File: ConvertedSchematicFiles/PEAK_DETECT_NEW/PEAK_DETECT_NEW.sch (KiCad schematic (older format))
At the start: 17 parts, among them U1 uA741

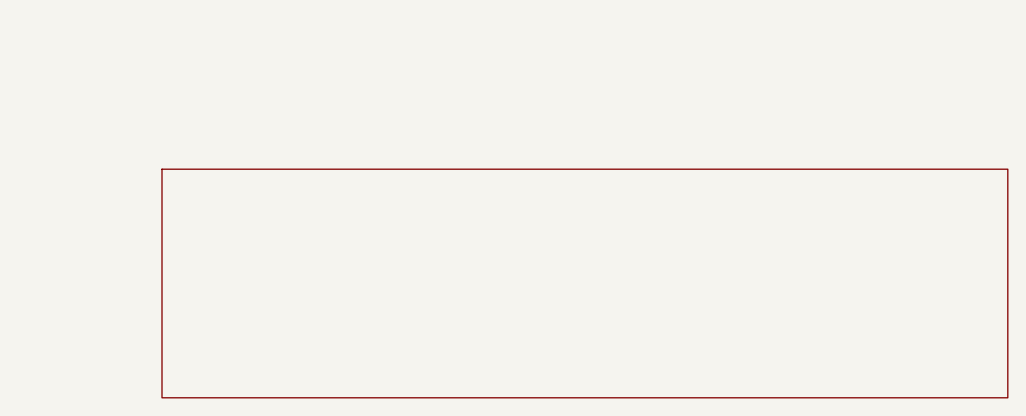
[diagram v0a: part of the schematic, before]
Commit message: Excluded some components. These no longer appear after conversion. When calling shell commands, filenames are in "quotes"
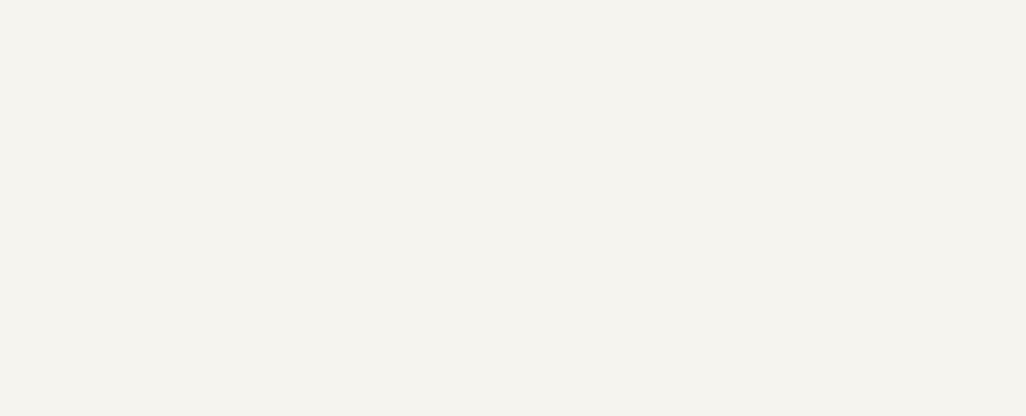
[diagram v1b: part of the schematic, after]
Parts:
- removed titleblk: titleblk, symbol TITLEBLK_PSPICE
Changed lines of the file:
@@
 	0    -1    1    0
-$EndComp
-$Comp
-L TITLEBLK_PSPICE titleblk
-U 1 1 25180540
-P 11880 8400
-F 0 "titleblk" H 23760 16800 30  0001 L CNN
-F 1 "titleblk" H 23760 16880 30  0001 L CNN
-	1    11880 8400
-	1    0    0    1
 $EndComp
 Wire Wire Line

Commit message: Ports issue fixed. Now annotation for ports is #PWR? function added "itos"
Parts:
- removed EGND (x6): EGND, symbol EGND_PSPICE
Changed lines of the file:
@@
 $EndDescr
 $Comp
-L EGND_PSPICE EGND
+L EGND_PSPICE #PWR1
 U 1 1 14289383
 P 2600 500
-F 0 "EGND" H 5200 1000 30  0001 L CNN
+F 0 "#PWR1" H 5200 1000 30  0001 L CNN
 F 1 "EGND" H 5200 1080 30  0001 L CNN
 	1    2600 500
@@
 $EndComp
 $Comp
-L EGND_PSPICE EGND
+L EGND_PSPICE #PWR2
 U 1 1 46930886
 P 1200 1700
-F 0 "EGND" H 2400 3400 30  0001 L CNN
+F 0 "#PWR2" H 2400 3400 30  0001 L CNN
 F 1 "EGND" H 2400 3480 30  0001 L CNN
 	1    1200 1700
@@
 $EndComp
 $Comp
-L EGND_PSPICE EGND
+L EGND_PSPICE #PWR3
 U 1 1 71692777
 P 3700 1800
-F 0 "EGND" H 7400 3600 30  0001 L CNN
+F 0 "#PWR3" H 7400 3600 30  0001 L CNN
 F 1 "EGND" H 7400 3680 30  0001 L CNN
 	1    3700 1800
@@
 $EndComp
 $Comp
-L EGND_PSPICE EGND
+L EGND_PSPICE #PWR4
 U 1 1 14636915
 P 2400 2200
-F 0 "EGND" H 4800 4400 30  0001 L CNN
+F 0 "#PWR4" H 4800 4400 30  0001 L CNN
 F 1 "EGND" H 4800 4480 30  0001 L CNN
 	1    2400 2200
@@
 $EndComp
 $Comp
-L EGND_PSPICE EGND
+L EGND_PSPICE #PWR5
 U 1 1 77747793
 P 3200 2500
-F 0 "EGND" H 6400 5000 30  0001 L CNN
+F 0 "#PWR5" H 6400 5000 30  0001 L CNN
 F 1 "EGND" H 6400 5080 30  0001 L CNN
 	1    3200 2500
@@
 $EndComp
 $Comp
-L EGND_PSPICE EGND
+L EGND_PSPICE #PWR6
 U 1 1 74238335
 P 3300 2100
-F 0 "EGND" H 6600 4200 30  0001 L CNN
+F 0 "#PWR6" H 6600 4200 30  0001 L CNN
 F 1 "EGND" H 6600 4280 30  0001 L CNN
 	1    3300 2100

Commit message: Added LICENSE.txt
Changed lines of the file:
@@
 $EndDescr
 $Comp
-L EGND_PSPICE #PWR1
+L GND #PWR1
 U 1 1 14289383
 P 2600 500
@@
 $EndComp
 $Comp
-L EGND_PSPICE #PWR2
+L GND #PWR2
 U 1 1 46930886
 P 1200 1700
@@
 $EndComp
 $Comp
-L EGND_PSPICE #PWR3
+L GND #PWR3
 U 1 1 71692777
 P 3700 1800
@@
 $EndComp
 $Comp
-L EGND_PSPICE #PWR4
+L GND #PWR4
 U 1 1 14636915
 P 2400 2200
@@
 $EndComp
 $Comp
-L EGND_PSPICE #PWR5
+L GND #PWR5
 U 1 1 77747793
 P 3200 2500
@@
 $EndComp
 $Comp
-L EGND_PSPICE #PWR6
+L GND #PWR6
 U 1 1 74238335
 P 3300 2100

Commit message: Orientation fix. Library components are now inverted, with +ve y axis going up. In Schematic files, +ve y axis is downwards. This is how the KiCad libraries are. As a result of the above fixed, the converted GND is now oriented correctly.
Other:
- moved on the sheet: U1, V1, V2, V3
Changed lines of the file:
@@
 F 1 "EGND" H 5200 1080 30  0001 L CNN
 	1    2600 500
-	1    0    0    1
+	1    0    0    -1
 $EndComp
 $Comp
@@
 F 1 "EGND" H 2400 3480 30  0001 L CNN
 	1    1200 1700
-	1    0    0    1
+	1    0    0    -1
 $EndComp
 $Comp
@@
 F 1 "EGND" H 7400 3680 30  0001 L CNN
 	1    3700 1800
-	1    0    0    1
+	1    0    0    -1
 $EndComp
 $Comp
@@
 F 1 "EGND" H 4800 4480 30  0001 L CNN
 	1    2400 2200
-	1    0    0    1
+	1    0    0    -1
 $EndComp
 $Comp
@@
 F 1 "EGND" H 6400 5080 30  0001 L CNN
 	1    3200 2500
-	1    0    0    1
+	1    0    0    -1
 $EndComp
 $Comp
@@
 F 1 "EGND" H 6600 4280 30  0001 L CNN
 	1    3300 2100
-	1    0    0    1
+	1    0    0    -1
 $EndComp
 $Comp
@@
 F 1 "15V" H 2400 790 30  0000 C CNN
 	1    2400 900
-	-1    0    0    -1
+	-1    0    0    1
 $EndComp
 $Comp
@@
 F 1 "VPWL" H 1200 1380 30  0000 L CNN
 	1    1200 1300
-	1    0    0    1
+	1    0    0    -1
 $EndComp
 $Comp
@@
 F 1 "-15V" H 2400 1690 30  0000 C CNN
 	1    2400 1800
-	1    0    0    1
+	1    0    0    -1
 $EndComp
 $Comp
@@
 F 1 "D1N4002" H 2900 1480 30  0000 L CNN
 	1    2900 1400
-	1    0    0    1
+	1    0    0    -1
 $EndComp
 $Comp
@@
 F 1 "10k" H 1600 2550 30  0000 L CNN
 	1    1600 2400
-	1    0    0    1
+	1    0    0    -1
 $EndComp
 $Comp
@@
 F 1 "D1N4002" H 3200 2580 30  0000 L CNN
 	1    3200 2500
-	0    1    -1    0
+	0    -1    -1    0
 $EndComp
 $Comp
@@
 F 1 "10U" H 3300 2250 30  0000 L CNN
 	1    3300 2100
-	0    1    -1    0
+	0    -1    -1    0
 $EndComp
 $Comp
@@
 F 1 "uA741" H 2000 1280 30  0000 L CNN
 	1    2000 1200
-	1    0    0    1
+	1    0    0    -1
 $EndComp
 $Comp
@@
 F 1 "10k" H 1200 1350 30  0000 L CNN
 	1    1200 1200
-	1    0    0    1
+	1    0    0    -1
 $EndComp
 $Comp
@@
 F 1 "100k" H 3700 1750 30  0000 L CNN
 	1    3700 1400
-	0    -1    1    0
+	0    1    1    0
 $EndComp
 Wire Wire Line

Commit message: Removed the use of exec, wrote basename function, made integration with eSim easier.
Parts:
- added titleblk: titleblk, symbol titleblk_PSPICE
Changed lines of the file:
@@
-EESchema Schematic File Version 2  date Wednesday 23 June 1999 12:03:41 AM IST
+EESchema Schematic File Version 2  date
 LIBS:power
 LIBS:device
@@
 LIBS:contrib
 LIBS:valves
-LIBS:ConvertedSchematicFiles/PEAK_DETECT_NEW-cache
 EELAYER 25  0
 EELAYER END
@@
 Sheet 1 1
 Title ""
-Date "23 Jun 1999"
+Date ""
 Rev ""
 Comp ""
@@
 	0    1    1    0
 $EndComp
+$Comp
+L titleblk_PSPICE titleblk
+U 1 1 25180540
+P 11880 8400
+F 0 "titleblk" H 23760 16800 30  0001 L CNN
+F 1 "titleblk" H 23760 16880 30  0001 L CNN
+	1    11880 8400
+	1    0    0    -1
+$EndComp
 Wire Wire Line
